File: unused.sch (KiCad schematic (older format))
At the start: 0 parts

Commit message: cont. work; all connections done now
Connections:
- no-connect marks 84 -> 63

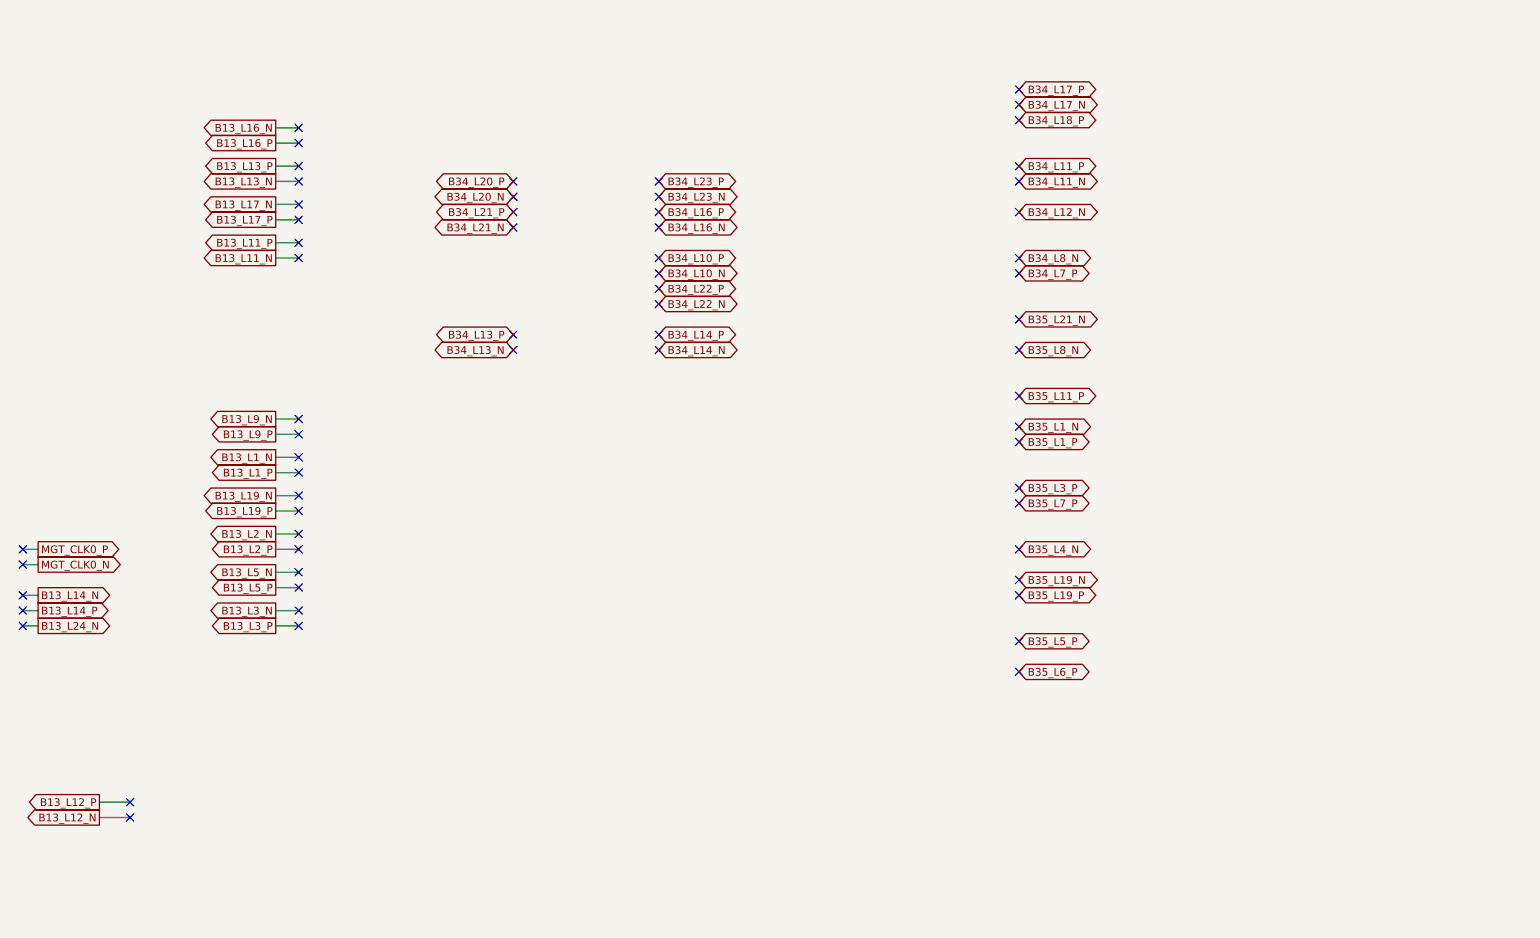
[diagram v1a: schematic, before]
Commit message: re-routed usbA (proper diff-pair); added mounting holes
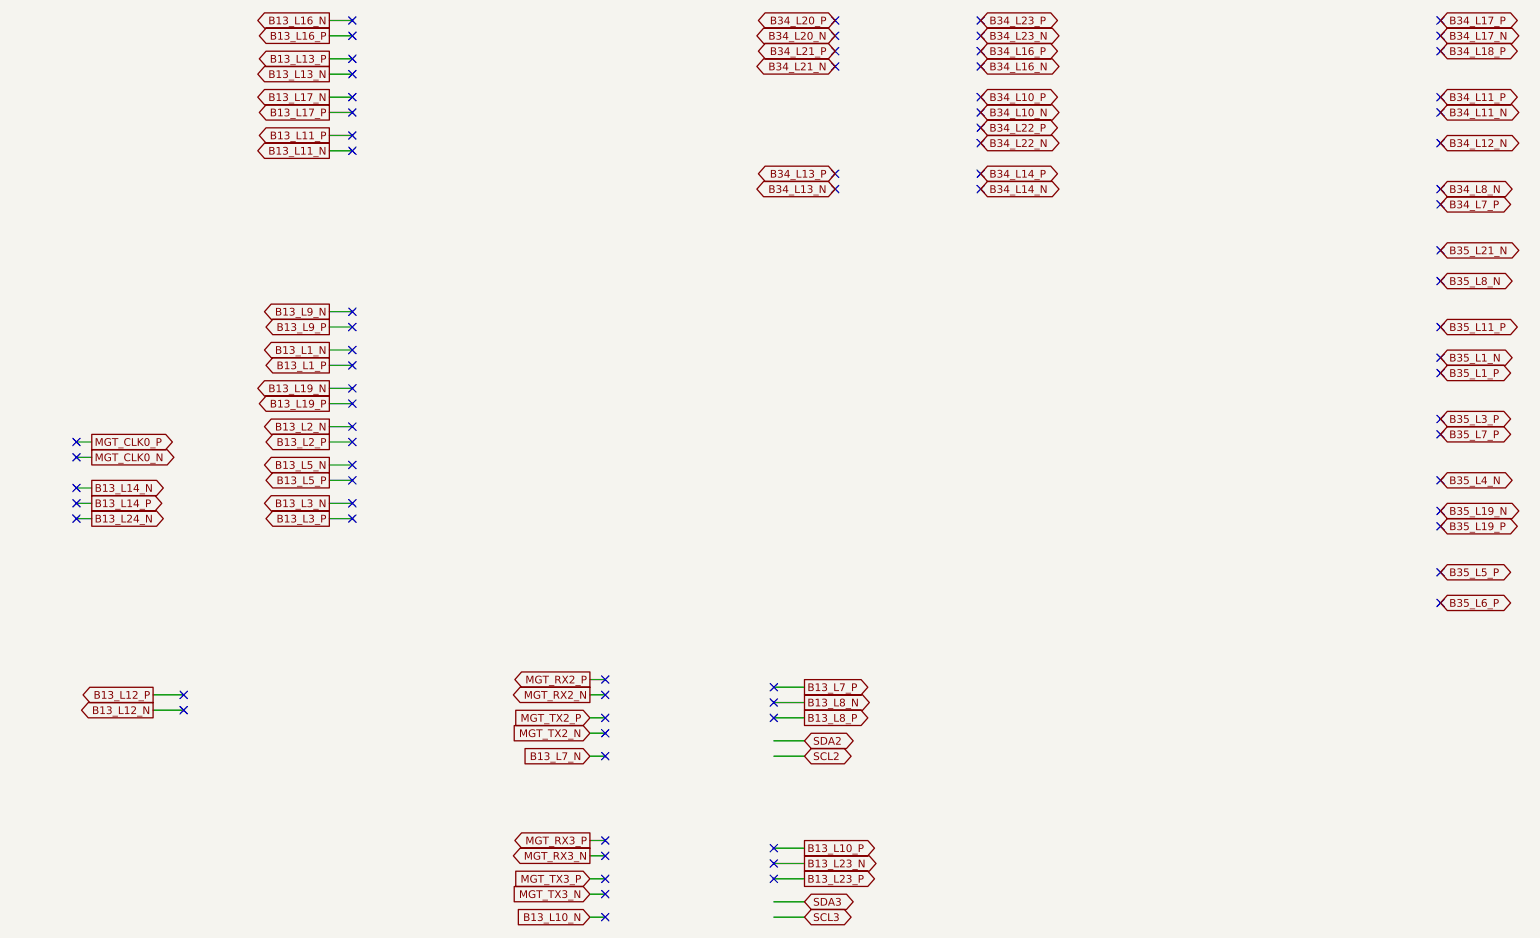
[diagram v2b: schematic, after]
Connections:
- net labels added: B13_L10_N, B13_L10_P, B13_L23_N, B13_L23_P, B13_L7_N, B13_L7_P, B13_L8_N, B13_L8_P, MGT_RX2_N, MGT_RX2_P, MGT_RX3_N, MGT_RX3_P, MGT_TX2_N, MGT_TX2_P, MGT_TX3_N, MGT_TX3_P, SCL2, SCL3, SDA2, SDA3
- wire segments 27 -> 47
- no-connect marks 63 -> 79

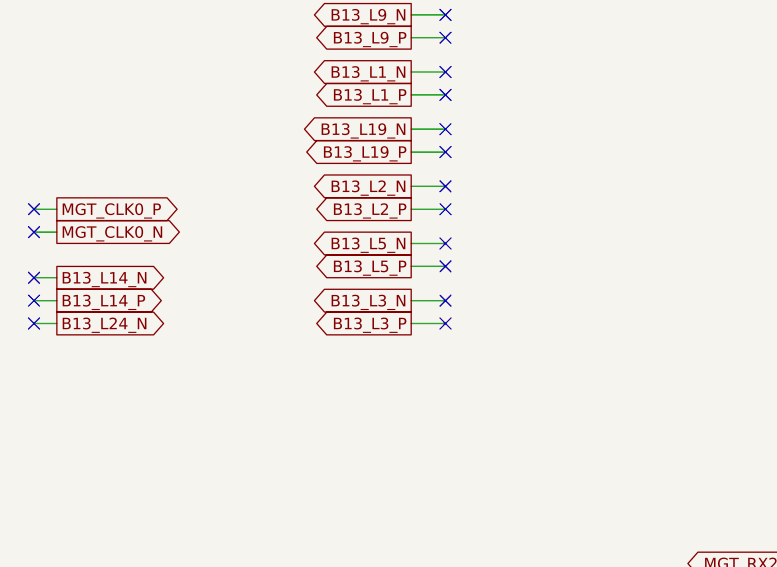
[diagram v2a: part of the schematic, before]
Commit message: use rj45/Gige + USB combo connector; hooked up LEDs
no more GND window under GigE diff-pairs on power-plane
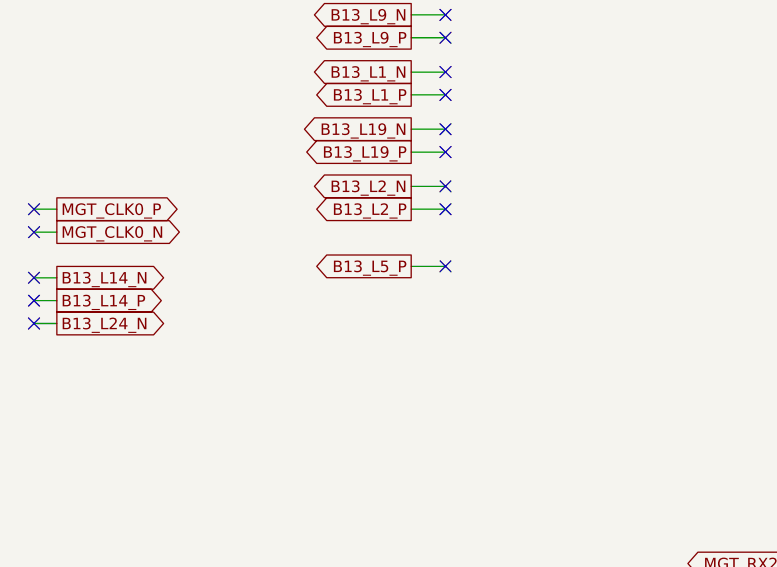
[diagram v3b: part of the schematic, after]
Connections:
- net labels removed: B13_L3_N, B13_L3_P, B13_L5_N
- wire segments 47 -> 44
- no-connect marks 79 -> 76
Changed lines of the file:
@@
 NoConn ~ 6200 2300
 NoConn ~ 6200 2400
-Text GLabel 2900 4450 0    50   Output ~ 0
-B13_L3_N
 Text GLabel 2900 4300 0    50   Output ~ 0
 B13_L5_P
-Text GLabel 2900 4200 0    50   Output ~ 0
-B13_L5_N
 Text GLabel 2900 3300 0    50   Output ~ 0
 B13_L9_P
@@
 Text GLabel 2900 1550 0    50   Output ~ 0
 B13_L13_P
-Text GLabel 2900 4550 0    50   Output ~ 0
-B13_L3_P
 Wire Wire Line
 	2900 3200 3050 3200
@@
 	2900 4050 3050 4050
 Wire Wire Line
-	2900 4200 3050 4200
-Wire Wire Line
 	2900 4300 3050 4300
-Wire Wire Line
-	2900 4450 3050 4450
-Wire Wire Line
-	2900 4550 3050 4550
 Wire Wire Line
 	2900 2150 3050 2150
@@
 NoConn ~ 3050 3950
 NoConn ~ 3050 4050
-NoConn ~ 3050 4200
 NoConn ~ 3050 4300
-NoConn ~ 3050 4450
-NoConn ~ 3050 4550
 Text GLabel 1350 4150 2    50   Output ~ 0
 MGT_CLK0_N

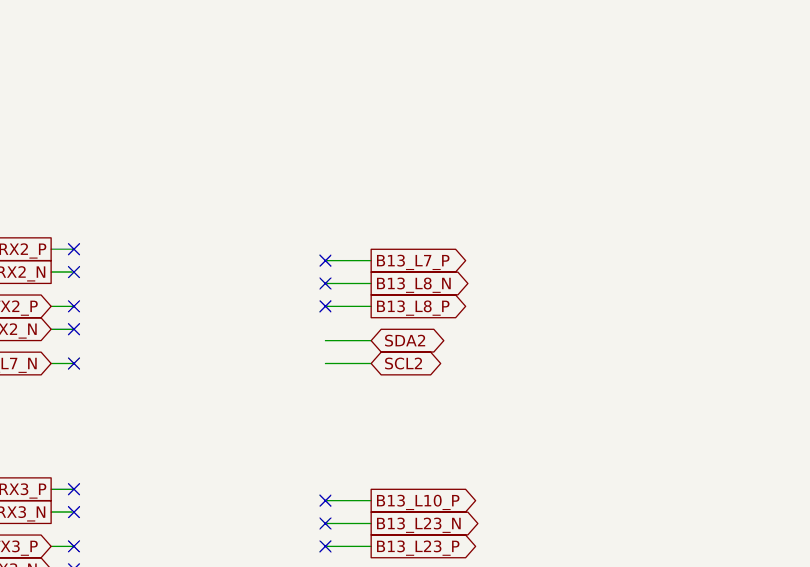
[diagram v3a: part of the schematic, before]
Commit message: Several changes; converging to prototype version 1.0.0
Added header for connecting external power-supply (in case
chips are not available)
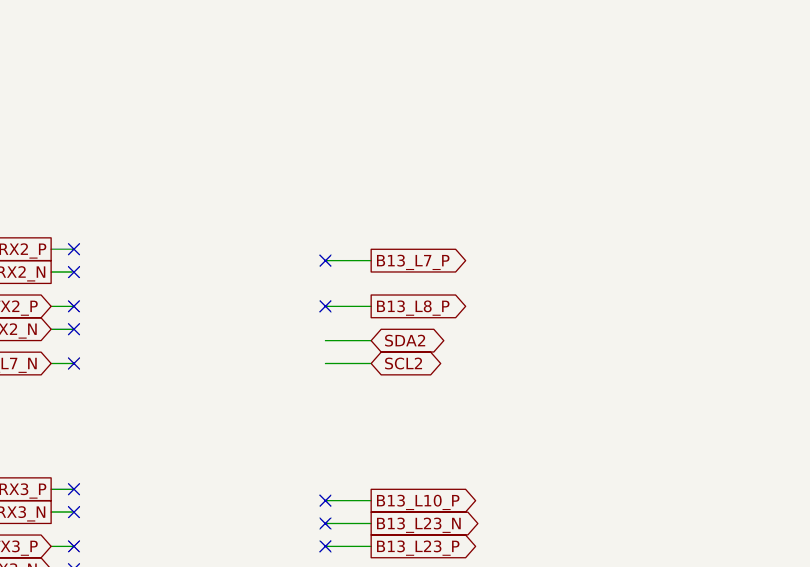
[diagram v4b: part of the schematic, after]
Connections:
- net labels removed: B13_L8_N
- wire segments 44 -> 43
- no-connect marks 76 -> 75
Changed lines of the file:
@@
 Text GLabel 6000 5850 2    50   Output ~ 0
 B13_L8_P
-Text GLabel 6000 5750 2    50   Output ~ 0
-B13_L8_N
 Text GLabel 6000 6700 2    50   Output ~ 0
 B13_L10_P
@@
 Wire Wire Line
 	5800 5650 6000 5650
-Wire Wire Line
-	5800 5750 6000 5750
 Wire Wire Line
 	5800 5850 6000 5850
@@
 NoConn ~ 5800 6900
 NoConn ~ 5800 5850
-NoConn ~ 5800 5750
 NoConn ~ 5800 5650
 $EndSCHEMATC
